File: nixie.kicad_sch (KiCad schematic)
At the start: 54 parts, among them IC1 SN74141, IC2 SN74141, IC3 SN74141, IC4 SN74141, IC5 MCP23017-E_SO, IC6 DS3231M+TRL, IC7 SN74141, IC8 SN74141, IC9 L7805CD2T-TR, J2 M20-9990646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

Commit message: Changes to schematic
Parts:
- removed J2: M20-9990646, HDRV6W64P0X254_1X6_1524X254X864P, symbol M20-9990646:M20-9990646
- added J1: M20-9990446, HDRV4W64P0X254_1X4_1016X254X889P, symbol M20-9990446:M20-9990446
- added R11: 10k, nixie:R0805, symbol nixie-eagle-import:R-US_R0805
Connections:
- net SWCLK is gone; now on net RST: U$1.GP2
- net +3V3: now also C12.1, R10.2, R5.2, R6.2, R9.2, J1.3, R11.2
- net +5V: no longer C12.1, R10.2, R5.2, R6.2, R9.2
- net GND: now also J1.4
- net RX: now also U$1.GP0, J1.1; no longer U$1.GP4
- net SCL: now also IC5.12 (SCL), R10.1; no longer U$1.GP1
- net SDA: now also IC5.13 (SDA), R9.1; no longer U$1.GP0
- net TX: now also U$1.GP1, J1.2; no longer U$1.GP5
- net RST: now reaches IC5.18 (~{RESET})
- net RST: now also R11.1
- removed net SCL1: IC5.12 (SCL), R10.1, U$1.GP7
- removed net SDA1: IC5.13 (SDA), R9.1, U$1.GP6
- net SWDIO: no longer names the net of U$1.GP3
- new net SCLIN: U$1.GP7
- new net SDAIN: U$1.GP6
- no-connect marks 3 -> 2

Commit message: Started routing
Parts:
- removed C12: 100nf, nixie:C0805, symbol nixie-eagle-import:C-USC0805
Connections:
- net SCLIN is gone; now on net A2: U$1.GP7
- net SDAIN is gone; now on net D2: U$1.GP6
- net A1: now also U$1.GP13; no longer IC5.1 (GPB0)
- net A2: no longer IC5.5 (GPB4)
- net A3: now also IC5.8 (GPB7); no longer IC5.28 (GPA7)
- net A4: now also IC5.1 (GPB0); no longer IC5.24 (GPA3)
- net A5: now also IC5.28 (GPA7); no longer U$1.GP8
- net A6: now also IC5.24 (GPA3); no longer U$1.GP12
- net B1: now also U$1.GP11; no longer IC5.2 (GPB1)
- net B2: now also U$1.GP5; no longer IC5.6 (GPB5)
- net B3: now also IC5.6 (GPB5); no longer IC5.27 (GPA6)
- net B4: now also IC5.3 (GPB2); no longer IC5.23 (GPA2)
- net B5: now also IC5.26 (GPA5); no longer U$1.GP9
- net B6: now also IC5.22 (GPA1); no longer U$1.GP13
- net C1: now also U$1.GP10; no longer IC5.3 (GPB2)
- net C2: now also U$1.GP4; no longer IC5.7 (GPB6)
- net C3: now also IC5.5 (GPB4); no longer IC5.26 (GPA5)
- net C4: now also IC5.4 (GPB3); no longer IC5.22 (GPA1)
- net C5: now also IC5.25 (GPA4); no longer U$1.GP10
- net C6: now also IC5.21 (GPA0); no longer U$1.GP14
- net D1: now also U$1.GP12; no longer IC5.4 (GPB3)
- net D2: no longer IC5.8 (GPB7)
- net D3: now also IC5.7 (GPB6); no longer IC5.25 (GPA4)
- net D4: now also IC5.2 (GPB1); no longer IC5.21 (GPA0)
- net D5: now also IC5.27 (GPA6); no longer U$1.GP11
- net D6: now also IC5.23 (GPA2); no longer U$1.GP15
- net S1: now also U$1.GP21; no longer U$1.GP16
- net S2: now also U$1.GP20; no longer U$1.GP17
- net S3: now also U$1.GP19; no longer U$1.GP18
- net S4: now also U$1.GP18; no longer U$1.GP19
- net S5: now also U$1.GP17; no longer U$1.GP20
- net S6: now also U$1.GP16; no longer U$1.GP21
- net SCL renamed SCL1
- net SCL1: now also U$1.GP15
- net SDA renamed SDA1
- net SDA1: now also U$1.GP14

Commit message: made minor changes to routing
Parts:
- S2: footprint PTS647SN50SMTR2LFS -> j2
- renumbered U$1 to P1
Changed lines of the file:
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@@
   (junction (at 317.5 35.56) (diameter 0) (color 0 0 0 0)
   )
-  (junction (at 349.25 93.98) (diameter 0) (color 0 0 0 0)
-  )
   (junction (at 185.42 102.87) (diameter 0) (color 0 0 0 0)
   )
@@
     (stroke (width 0.1524) (type solid))
   )
-  (wire (pts (xy 349.25 93.98) (xy 349.25 96.52))
-    (stroke (width 0) (type default))
-  )
   (wire (pts (xy 78.74 214.63) (xy 73.66 214.63))
     (stroke (width 0.1524) (type solid))
@@
     (stroke (width 0) (type default))
   )
-  (wire (pts (xy 349.25 92.71) (xy 349.25 93.98))
-    (stroke (width 0) (type default))
-  )
   (wire (pts (xy 139.7 156.21) (xy 134.62 156.21))
     (stroke (width 0.1524) (type solid))
@@
     (stroke (width 0.1524) (type solid))
   )
+  (wire (pts (xy 349.25 92.71) (xy 349.25 96.52))
+    (stroke (width 0) (type default))
+  )
   (wire (pts (xy 312.42 154.94) (xy 312.42 157.48))
     (stroke (width 0) (type default))
@@
       (effects (font (size 1.27 1.27)))
     )
-    (property "Footprint" "PTS647SN50SMTR2LFS" (at 370.84 177.47 0)
+    (property "Footprint" "j2" (at 370.84 177.47 0)
       (effects (font (size 1.27 1.27)) (justify left top) hide)
     )
@@
     )
   )
-  (symbol (lib_id "power:+3V3") (at 349.25 93.98 0) (unit 1)
+  (symbol (lib_id "power:+3V3") (at 349.25 92.71 0) (unit 1)
     (in_bom yes) (on_board yes) (dnp no) (fields_autoplaced)
-    (property "Reference" "#PWR031" (at 349.25 97.79 0)
+    (property "Reference" "#PWR031" (at 349.25 96.52 0)
       (effects (font (size 1.27 1.27)) hide)
     )
-    (property "Value" "+3V3" (at 349.25 88.9 0)
+    (property "Value" "+3V3" (at 349.25 87.63 0)
       (effects (font (size 1.27 1.27)))
     )
-    (property "Footprint" "" (at 349.25 93.98 0)
+    (property "Footprint" "" (at 349.25 92.71 0)
       (effects (font (size 1.27 1.27)) hide)
     )
-    (property "Datasheet" "" (at 349.25 93.98 0)
+    (property "Datasheet" "" (at 349.25 92.71 0)
       (effects (font (size 1.27 1.27)) hide)
     )
@@
   (symbol (lib_id "nixie-eagle-import:RPI_PICO-TH") (at 60.96 57.15 0) (unit 1)
     (in_bom yes) (on_board yes) (dnp no)
-    (property "Reference" "U$1" (at 60.96 26.67 0)
-      (effects (font (size 2.54 2.159)) hide)
+    (property "Reference" "P1" (at 60.96 26.67 0)
+      (effects (font (size 2.54 2.159)))
     )
     (property "Value" "RPI_PICO-TH" (at 60.96 21.59 0)
@@
       (project "nixie"
         (path "/ba431371-aaad-4536-8520-64dab3af26c3"
-          (reference "U$1") (unit 1)
+          (reference "P1") (unit 1)
         )
       )

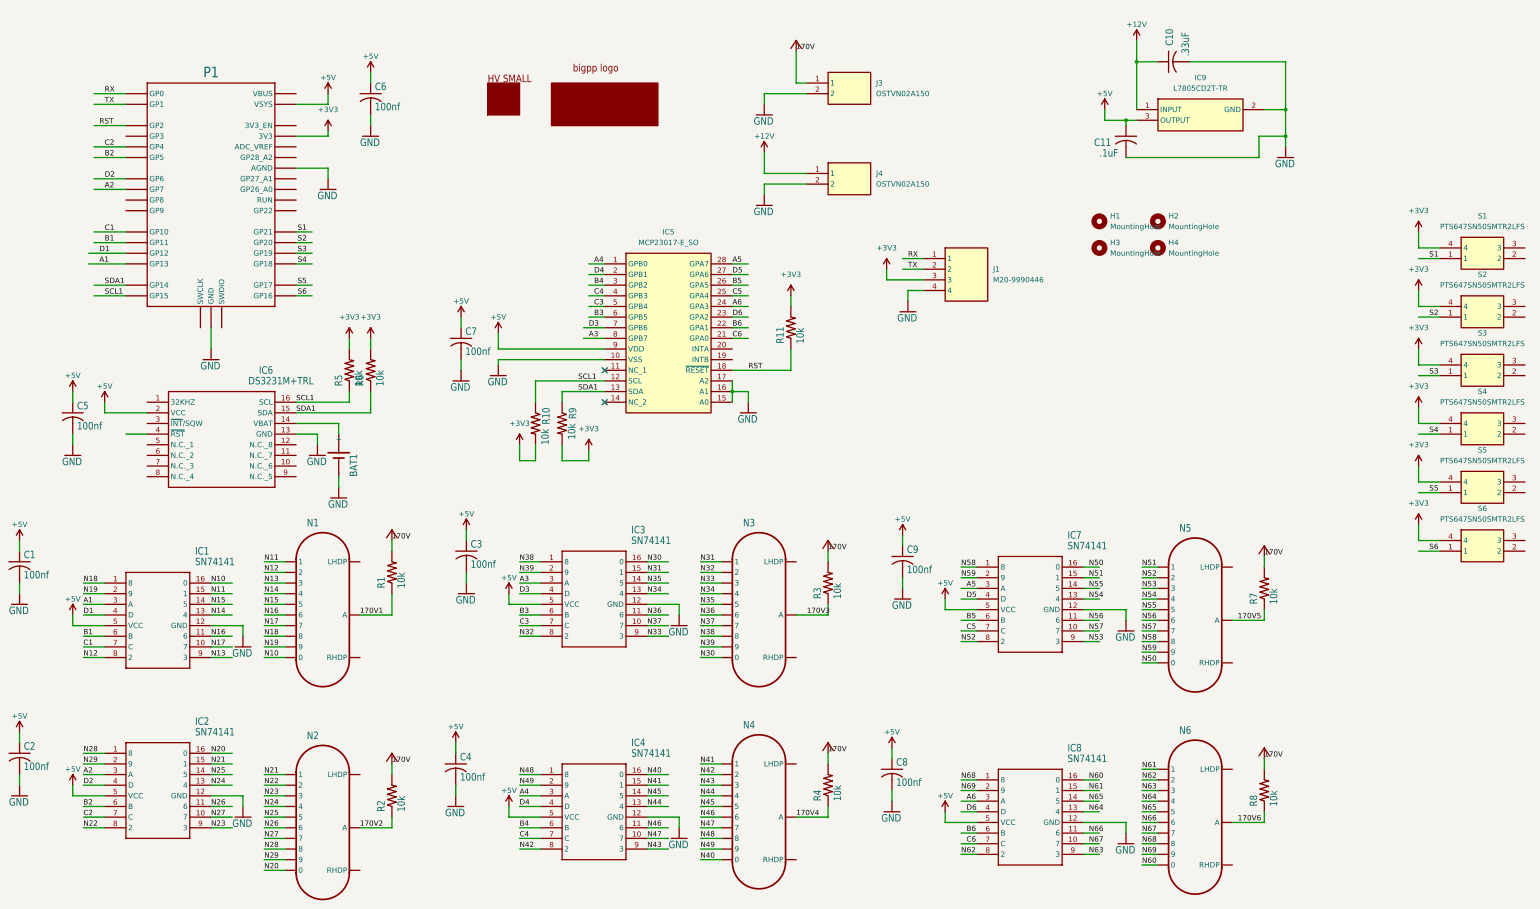
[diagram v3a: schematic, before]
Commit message: added reset line for clock
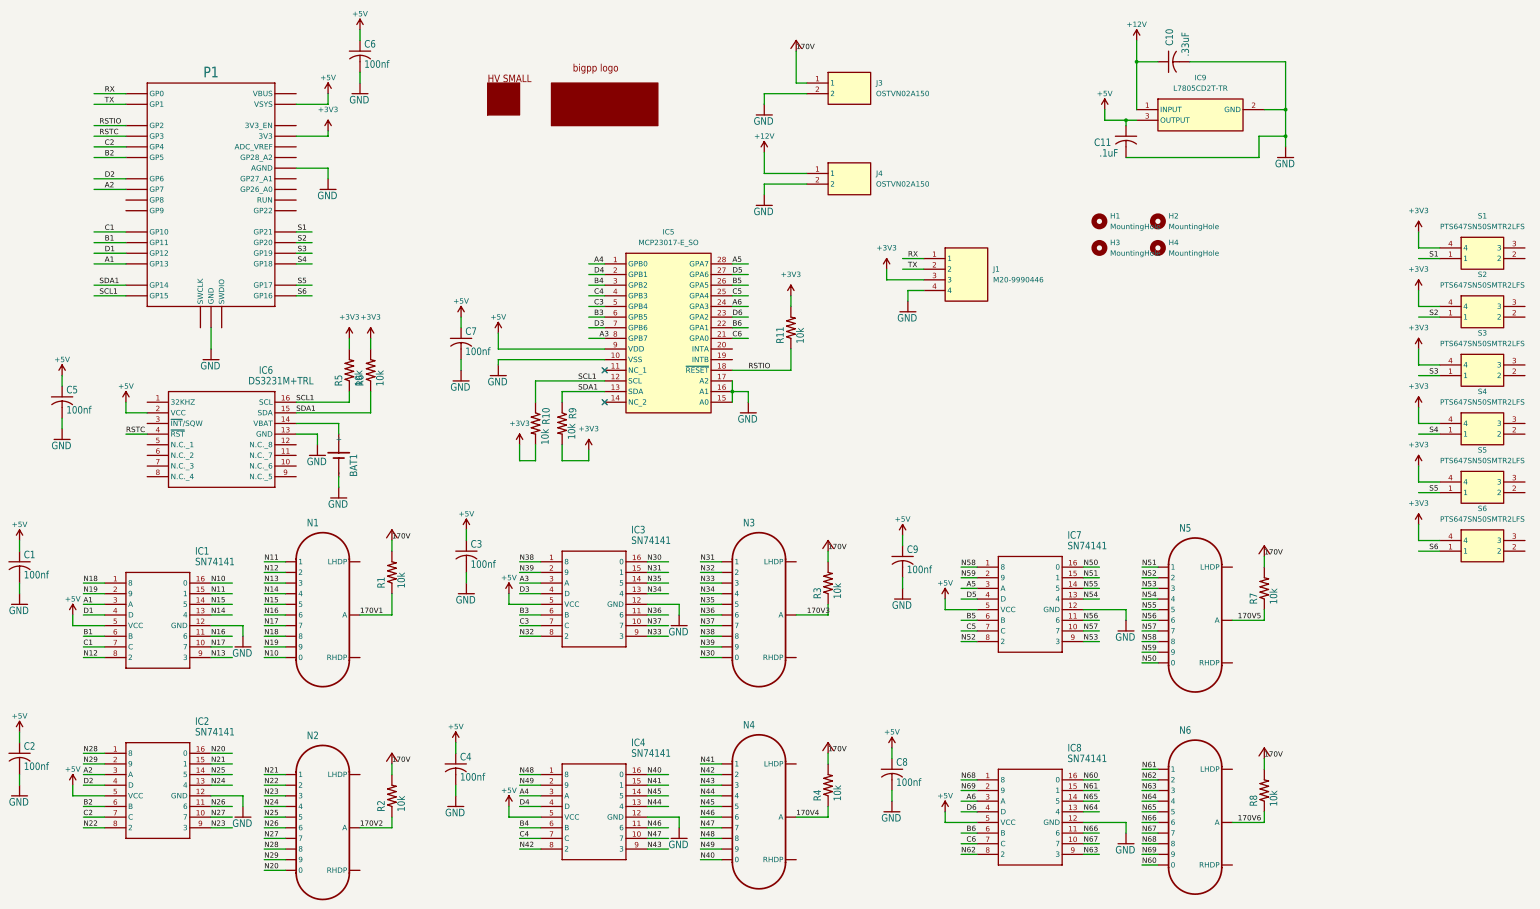
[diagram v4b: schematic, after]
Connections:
- net RSTC: now reaches IC6.4 (~{RST})
- net RSTC: now also P1.GP3
- net RST renamed RSTIO
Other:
- moved on the sheet: C5, C6
